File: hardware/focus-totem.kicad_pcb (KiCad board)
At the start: 2 copper layers, 13 parts, among them J1 SSD1306_0.91, SW1 SW_Push, SW2 SW_Push, SW3 SW_Push, SW4 EC11, U1 XIAO-RP2040

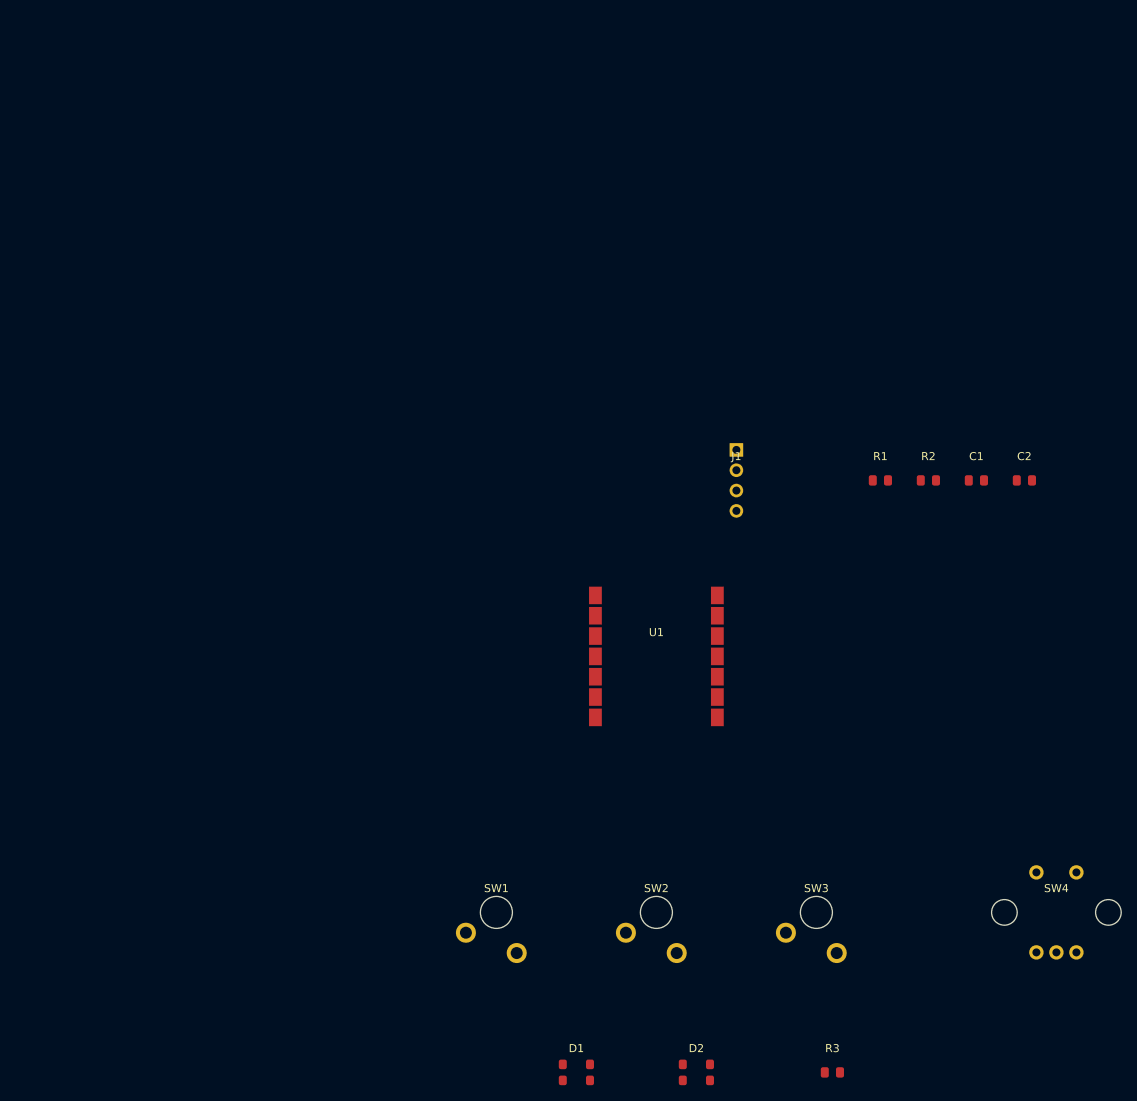
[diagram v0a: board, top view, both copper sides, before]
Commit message: Added Pomodoro timer, RGB/OLED, and updates
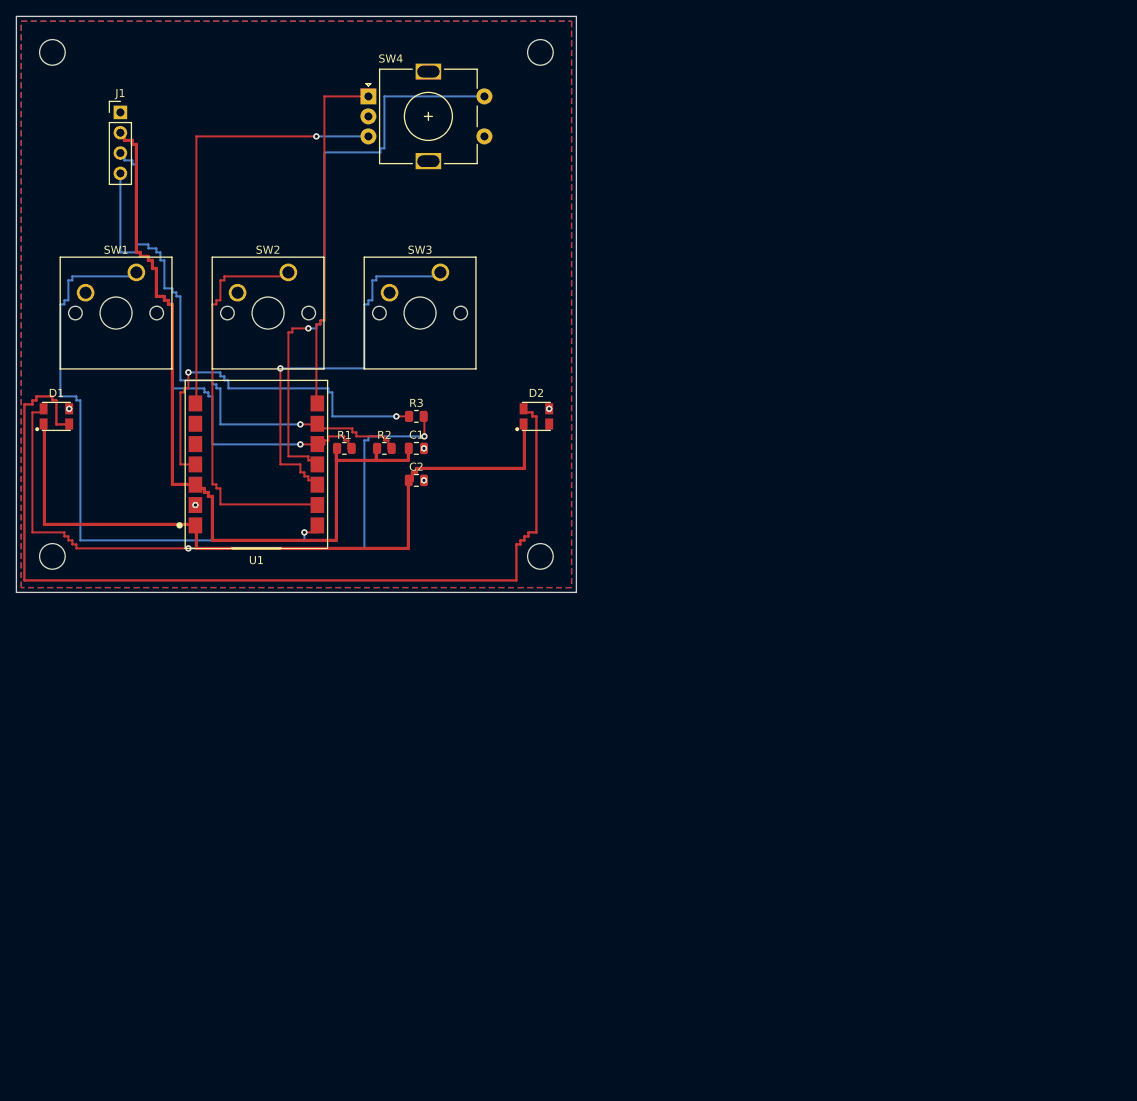
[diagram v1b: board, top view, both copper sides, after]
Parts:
- added H1: MountingHole, MountingHole:MountingHole_3.2mm_M3, F.Cu at (24.5, 24.5)
- added H2: MountingHole, MountingHole:MountingHole_3.2mm_M3, F.Cu at (85.5, 24.5)
- added H3: MountingHole, MountingHole:MountingHole_3.2mm_M3, F.Cu at (24.5, 87.5)
- added H4: MountingHole, MountingHole:MountingHole_3.2mm_M3, F.Cu at (85.5, 87.5)
- D1, D2: footprint SK6812MINI-E:SK6812MINI-E -> focus-totem:SK6812MINI-E
- SW1, SW2, SW3: footprint Button_Switch_Keyboard:SW_Cherry_MX_1.00u -> Button_Switch_Keyboard:SW_Cherry_MX_1.00u_PCB
- SW4: footprint Rotary_Encoder:RotaryEncoder_Alps_EC11E-Switch -> Rotary_Encoder:RotaryEncoder_Alps_EC11E-Switch_Vertical_H20mm
- U1: footprint XIAO-RP2040:XIAO-RP2040 -> focus-totem:XIAO-RP2040
- moved SW4 133.4 mm to (64.0, 30.0)
- moved D1 104.6 mm to (25.0, 70.0)
- moved R3 97.1 mm to (70.0, 70.0)
- moved SW3 92.8 mm to (73.0, 52.0)
- moved SW2 92.3 mm to (54.0, 52.0)
- moved SW1 91.8 mm to (35.0, 52.0)
- moved J1 89.7 mm to (33.0, 32.0)
- moved D2 84.4 mm to (85.0, 70.0)
- moved C2 76.0 mm to (70.0, 78.0)
- moved C1 70.1 mm to (70.0, 74.0)
- moved R2 68.1 mm to (66.0, 74.0)
- moved R1 67.1 mm to (61.0, 74.0)
- moved U1 55.5 mm to (50.0, 76.0), turned to 180 degrees
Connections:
- D2 pad 2: DOUT2 -> unconnected-(D2-DOUT-Pad2)
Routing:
- net DOUT1: track 0.00 -> 119.0 mm
- net +3V3: track 0.00 -> 104.5 mm
- net +5V: track 0.00 -> 91.0 mm
- net DIN1: track 0.00 -> 84.5 mm, vias 0 -> 2
- net KEY1: track 0.00 -> 77.0 mm, vias 0 -> 1
- net ENC_SW: track 0.00 -> 74.0 mm, vias 0 -> 1
- net SCL: track 0.00 -> 71.0 mm, vias 0 -> 1
- net SDA: track 0.00 -> 65.5 mm, vias 0 -> 1
- net ENC_B: track 0.00 -> 55.0 mm, vias 0 -> 1
- net KEY2: track 0.00 -> 51.5 mm
- net KEY3: track 0.00 -> 51.0 mm, vias 0 -> 1
- net DATA_RAW: track 0.00 -> 47.5 mm, vias 0 -> 2
- net ENC_A: track 0.00 -> 45.0 mm
- net GND: vias 0 -> 5
- added copper zone on B.Cu, net GND
- added copper zone on F.Cu, net GND
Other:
- board outline added: 70 x 72 mm
- rule pad_to_mask_clearance: 0.0 -> 0

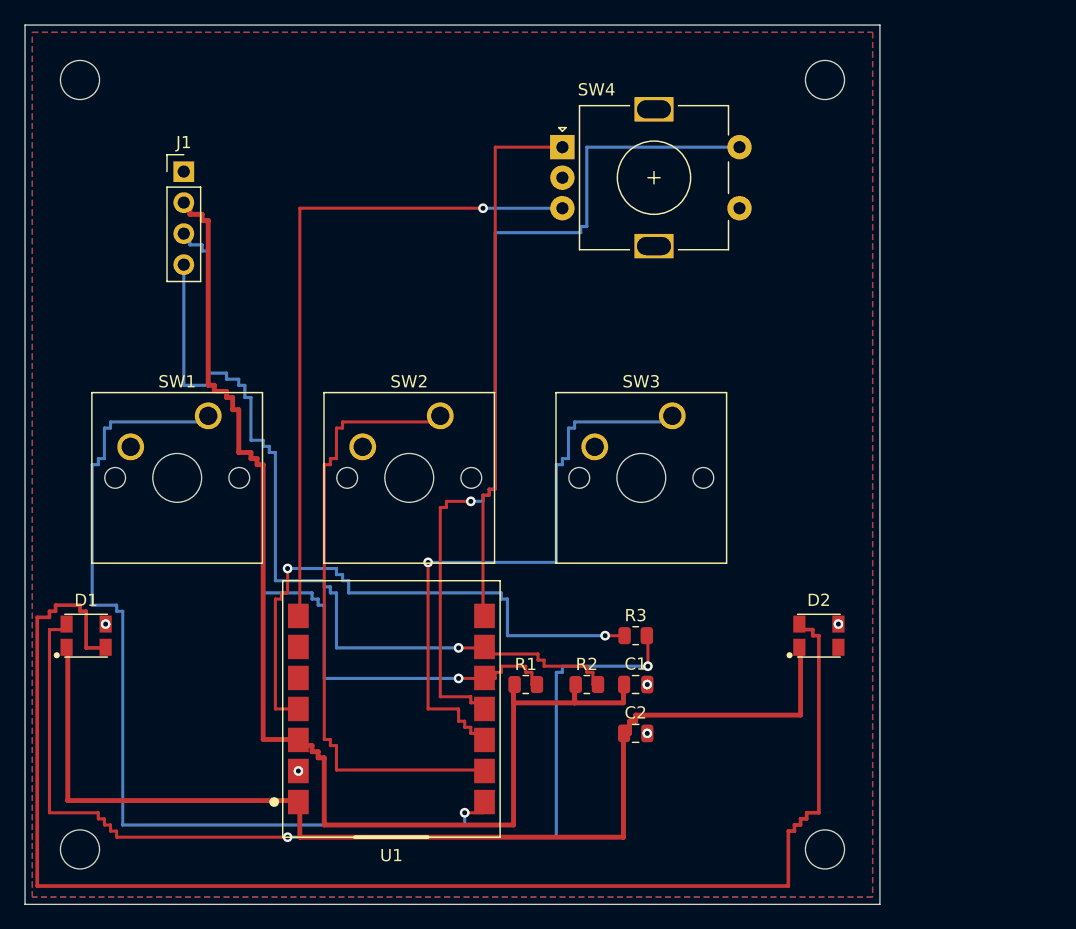
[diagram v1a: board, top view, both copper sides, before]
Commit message: Add case files and update README
Add the case TLs (plate + bottom), and updated Readme
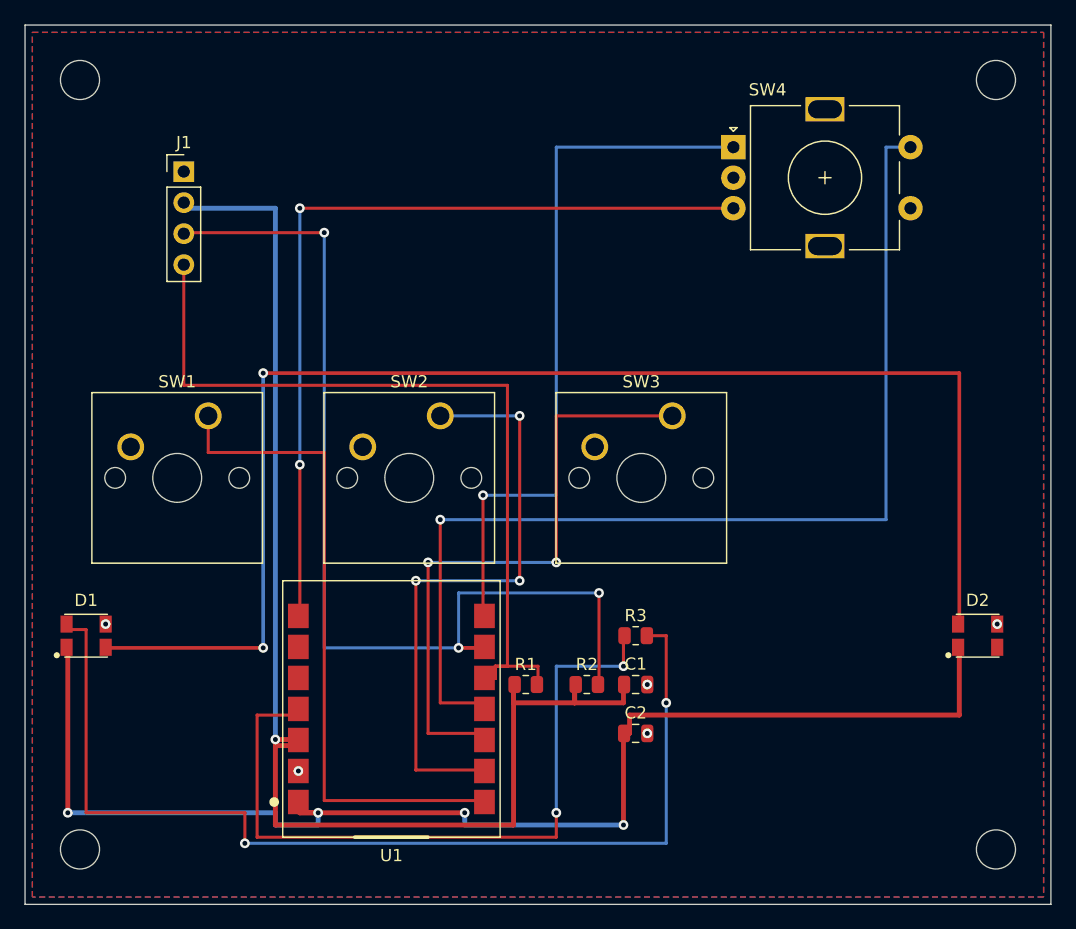
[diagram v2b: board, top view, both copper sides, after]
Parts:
- moved H2 14.0 mm to (99.5, 24.5)
- moved H4 14.0 mm to (99.5, 87.5)
- moved SW4 14.0 mm to (78.0, 30.0)
- moved D2 13.0 mm to (98.0, 70.0)
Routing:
- net KEY1: track 77.0 -> 54.0 mm, vias 1 -> 0
- net +5V: track 91.0 -> 109.0 mm, vias 0 -> 4
- net ENC_SW: track 74.0 -> 88.0 mm
- net ENC_B: track 55.0 -> 69.0 mm, vias 1 -> 2
- net ENC_A: track 45.0 -> 59.0 mm, vias 0 -> 1
- net SCL: track 71.0 -> 84.0 mm, vias 1 -> 3
- net DATA_RAW: track 47.5 -> 60.5 mm
- net DOUT1: track 119.0 -> 113.0 mm, vias 0 -> 2
- net SDA: track 65.5 -> 69.5 mm, vias 1 -> 0
- net +3V3: track 104.5 -> 108.5 mm, vias 0 -> 1
- net KEY2: track 51.5 -> 49.5 mm, vias 0 -> 3
- net DIN1: track 84.5 -> 85.5 mm
- net KEY3: vias 1 -> 2
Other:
- board size 70 x 72 mm -> 84 x 72 mm
